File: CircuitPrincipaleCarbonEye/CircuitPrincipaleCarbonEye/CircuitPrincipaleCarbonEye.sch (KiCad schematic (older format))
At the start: 18 parts, among them J1 Conn_01x01_Male, Q1 Q_PMOS_DGS, Q2 Q_NMOS_DGS, U1 OPA4227PA, U2 ADS1115, U3 GROOVE, U4 molex4-pin

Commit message: post premier_test
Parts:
- U1: symbol OPA4227PA:OPA4227PA -> CircuitPrincipaleCarbonEye-rescue:OPA4227PA-OPA4227PA
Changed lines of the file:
@@
 $EndComp
 $Comp
-L OPA4227PA:OPA4227PA U1
+L CircuitPrincipaleCarbonEye-rescue:OPA4227PA-OPA4227PA U1
 U 1 1 60D4A1CB
 P 2950 1100

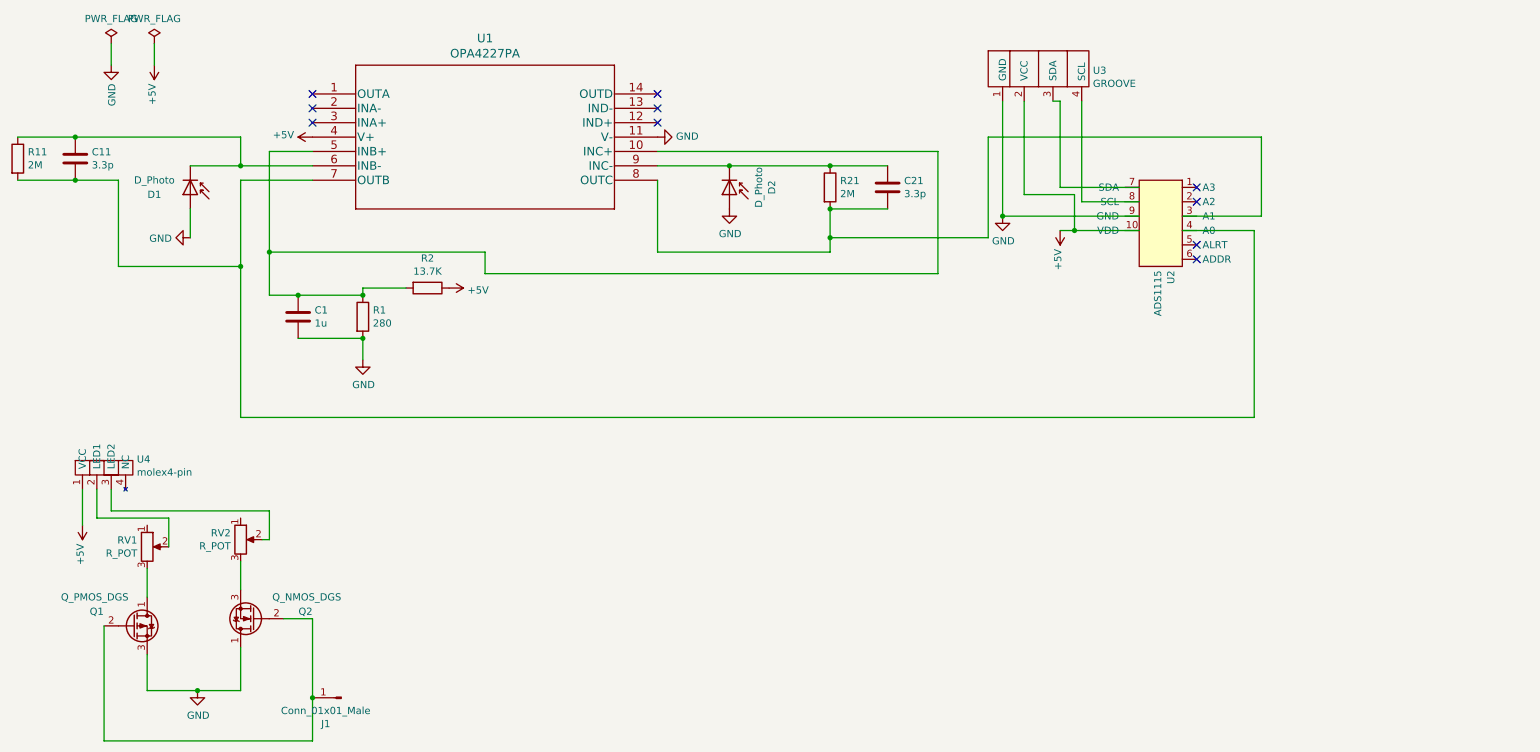
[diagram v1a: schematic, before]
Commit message: ADC 24bits, SPI
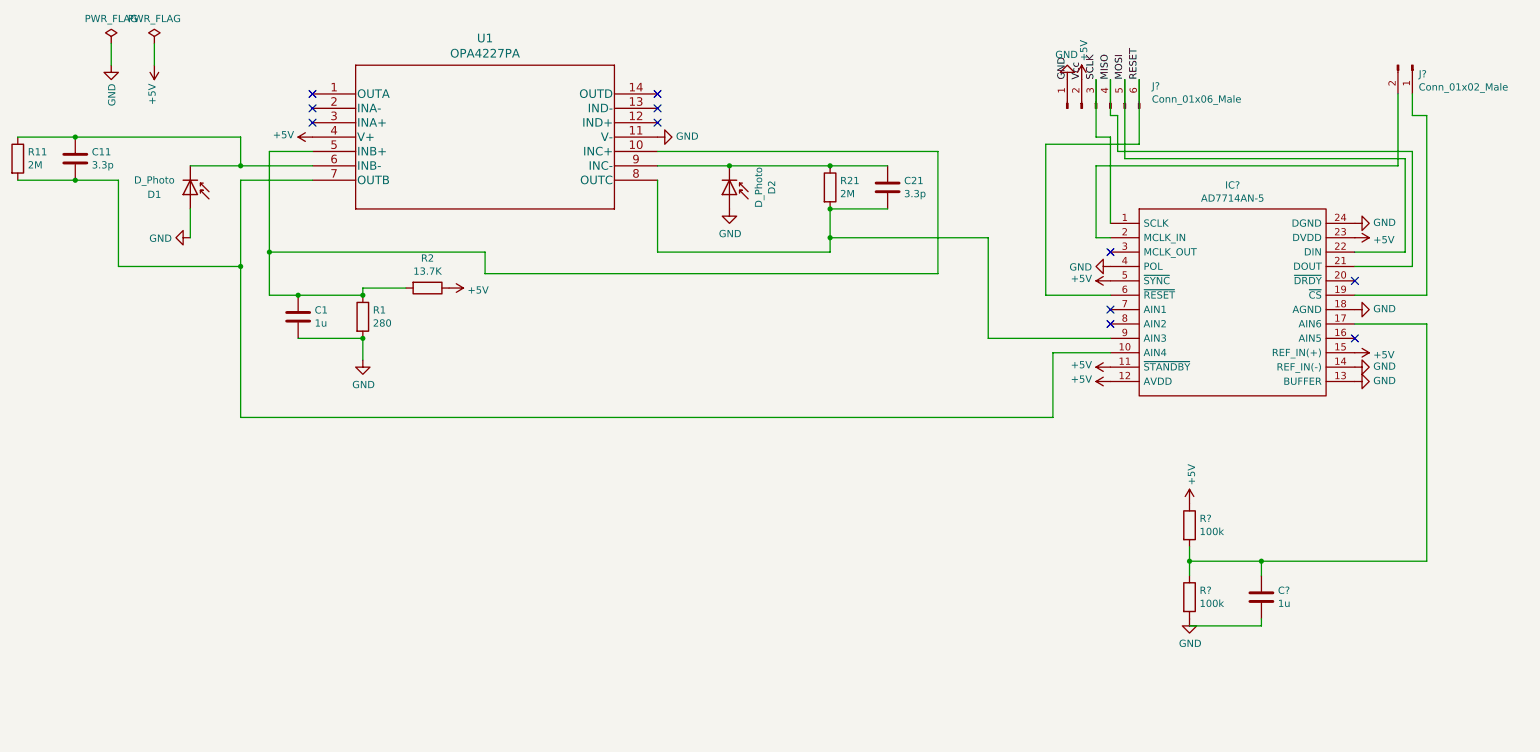
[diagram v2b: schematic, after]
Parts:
- removed J1: Conn_01x01_Male, symbol Connector:Conn_01x01_Male
- removed Q1: Q_PMOS_DGS, symbol Device:Q_PMOS_DGS
- removed Q2: Q_NMOS_DGS, symbol Device:Q_NMOS_DGS
- removed RV1, RV2: R_POT, symbol Device:R_POT
- removed U2: ADS1115, symbol CircuitPrincipaleCarbonEye-rescue:ADS1115-LibrairieCarbonEye
- removed U3: GROOVE, symbol CircuitPrincipaleCarbonEye-rescue:GROOVE4-pin-LibrairieCarbonEye
- removed U4: molex4-pin, symbol CircuitPrincipaleCarbonEye-rescue:molex4-pin-LibrairieCarbonEye
- added C?: 1u, Capacitor_THT:C_Disc_D8.0mm_W2.5mm_P5.00mm, symbol Device:C
- added IC?: AD7714AN-5, DIP787W50P254L3116H762Q24N, symbol SamacSys_Parts:AD7714AN-5
- added J?: Conn_01x06_Male, symbol Connector:Conn_01x06_Male
- added J?: Conn_01x02_Male, symbol Connector:Conn_01x02_Male
- added R? (x2): 100k, symbol Device:R
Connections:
- net +5V: now also IC?.11 (~STANDBY), IC?.12 (AVDD), IC?.15 (REF_IN(+)), IC?.23 (DVDD), IC?.5 (~SYNC), J?.2 (Pin_2), R?.1
- net GND: now also IC?.13 (BUFFER), IC?.14 (REF_IN(-)), IC?.18 (AGND), IC?.24 (DGND), IC?.4 (POL), J?.1 (Pin_1), R?.2
- net at C11.2, R11.2, U1.7 (OUTB): now also IC?.10 (AIN4)
- net at C21.2, R21.2, U1.8 (OUTC): now also IC?.9 (AIN3)
- new net: C?.1, IC?.17 (AIN6), R?.1, R?.2
- new net: IC?.19 (~CS), J?.1 (Pin_1)
- new net: IC?.2 (MCLK_IN), J?.2 (Pin_2)
- new net MISO: IC?.21 (DOUT), J?.4 (Pin_4)
- new net MOSI: IC?.22 (DIN), J?.5 (Pin_5)
- new net RESET: IC?.6 (~RESET), J?.6 (Pin_6)
- new net SCLK: IC?.1 (SCLK), J?.3 (Pin_3)
- no-connect marks 10 -> 11
